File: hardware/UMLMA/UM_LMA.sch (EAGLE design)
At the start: 14 parts, among them IC1 TINY25, J1 AVRISP6_TP

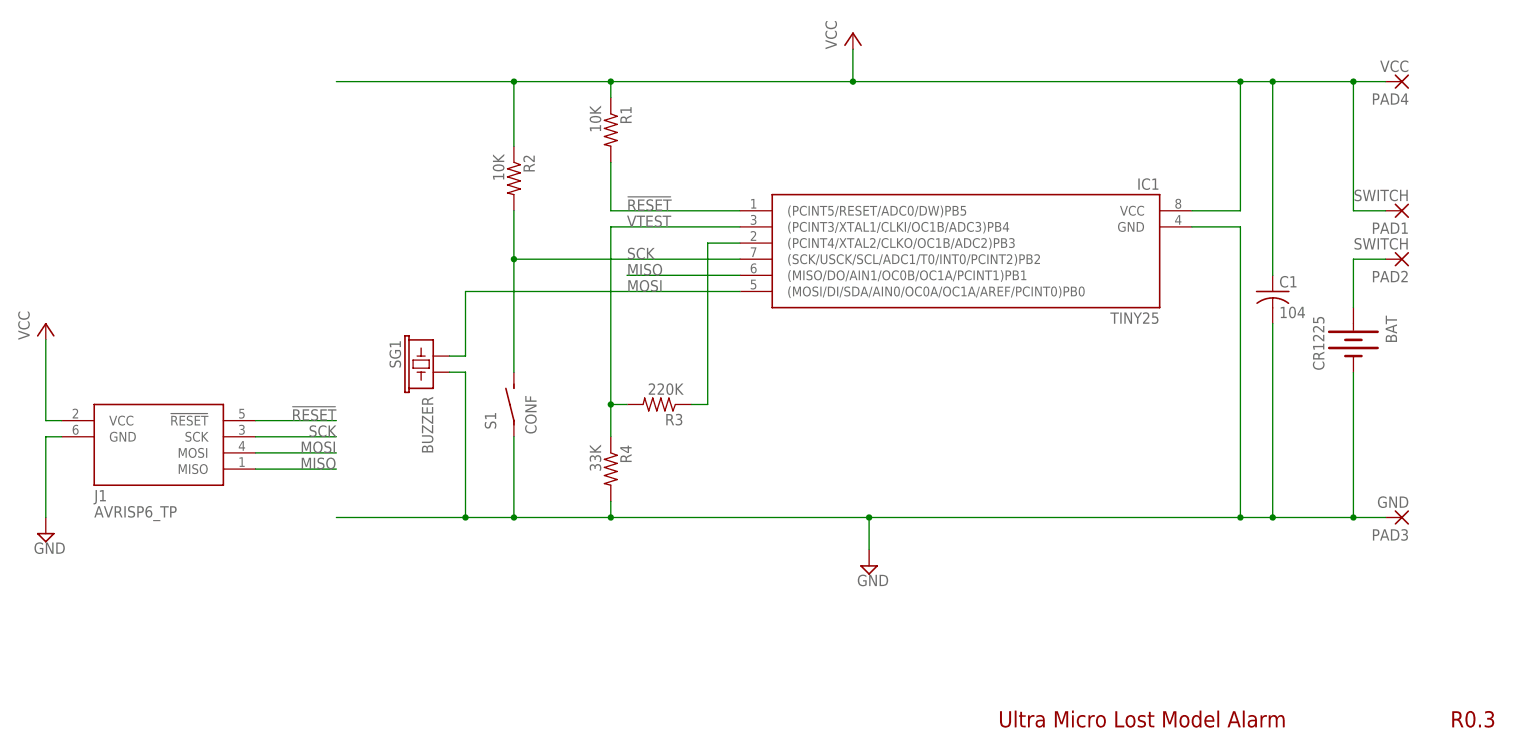
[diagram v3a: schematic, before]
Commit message: Removed extraneous switch pull-up resistor, moved layout and silk labels, increased switch footprint sizes, updated gerbers
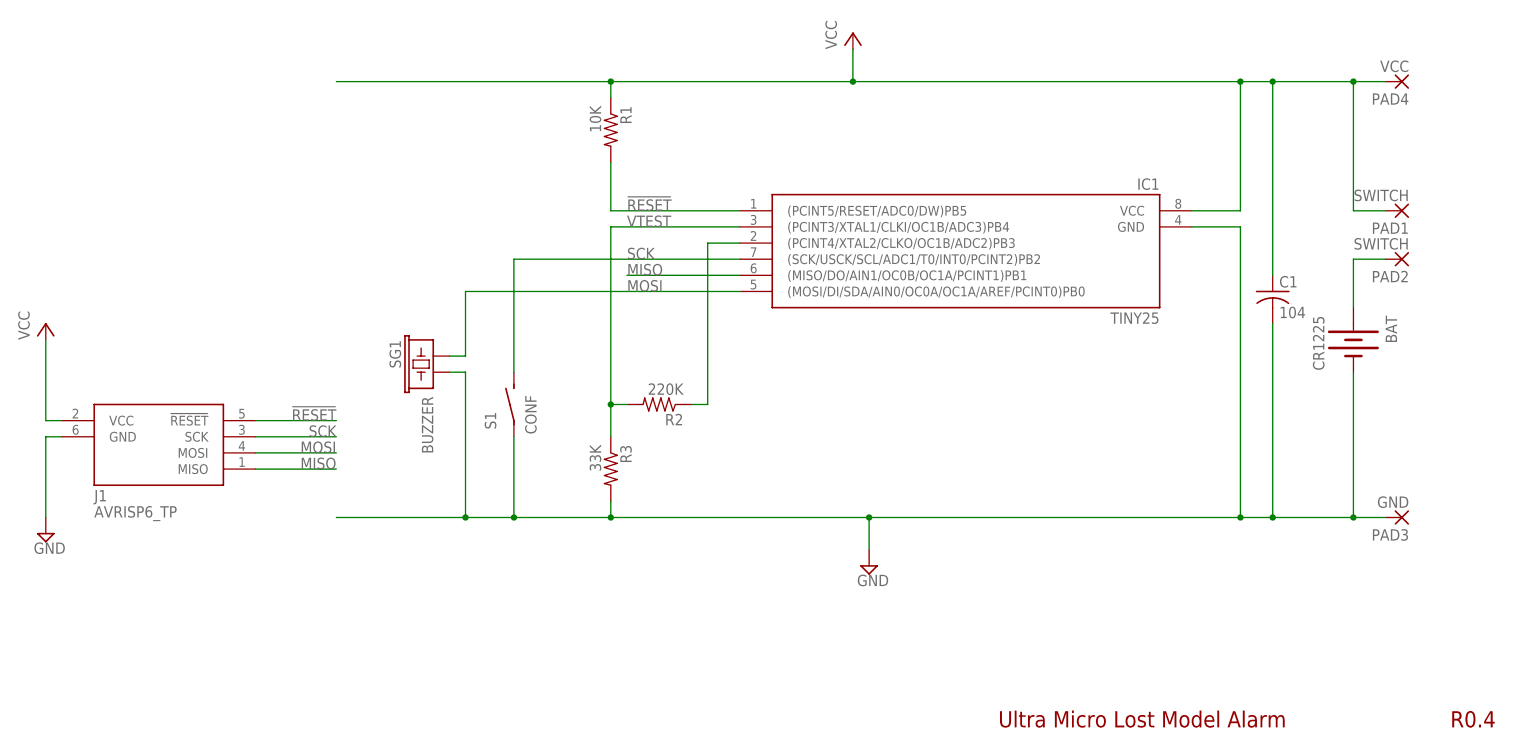
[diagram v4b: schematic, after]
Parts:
- removed R4: 33K, rcl:R-US_R0603
- R2: value 10K -> 220K
- R3: value 220K -> 33K
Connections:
- net GND: now also R3.2; no longer R4.2
- net N$5: now also R2.1; no longer R3.1
- net SCK: no longer R2.2
- net VCC: no longer R2.1
- net VTEST: now also R2.2, R3.1; no longer R3.2, R4.1
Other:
- note added: "R0.4"
- note removed: "R0.3"
- moved on the sheet: R2, R3
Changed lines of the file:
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@@
 <layer number="54" name="bGND_GNDA" color="1" fill="9" visible="no" active="no"/>
 <layer number="56" name="wert" color="7" fill="1" visible="no" active="no"/>
+<layer number="57" name="tCAD" color="7" fill="1" visible="no" active="no"/>
+<layer number="59" name="tCarbon" color="7" fill="1" visible="no" active="no"/>
+<layer number="60" name="bCarbon" color="7" fill="1" visible="no" active="no"/>
+<layer number="90" name="Modules" color="5" fill="1" visible="no" active="no"/>
 <layer number="91" name="Nets" color="2" fill="1" visible="yes" active="yes"/>
 <layer number="92" name="Busses" color="1" fill="1" visible="yes" active="yes"/>
@@
 <layer number="97" name="Info" color="7" fill="1" visible="yes" active="yes"/>
 <layer number="98" name="Guide" color="6" fill="1" visible="yes" active="yes"/>
+<layer number="99" name="SpiceOrder" color="7" fill="1" visible="no" active="no"/>
 <layer number="100" name="Muster" color="7" fill="1" visible="no" active="no"/>
 <layer number="101" name="Hidden" color="15" fill="1" visible="yes" active="yes"/>
@@
 <layer number="106" name="bPlate" color="7" fill="1" visible="yes" active="yes"/>
 <layer number="107" name="Crop" color="7" fill="1" visible="yes" active="yes"/>
+<layer number="108" name="tplace-old" color="10" fill="1" visible="no" active="yes"/>
+<layer number="109" name="ref-old" color="11" fill="1" visible="no" active="yes"/>
+<layer number="110" name="fp0" color="7" fill="1" visible="no" active="yes"/>
+<layer number="111" name="LPC17xx" color="7" fill="1" visible="no" active="yes"/>
+<layer number="113" name="IDFDebug" color="4" fill="1" visible="no" active="yes"/>
 <layer number="116" name="Patch_BOT" color="9" fill="4" visible="yes" active="yes"/>
 <layer number="121" name="_tsilk" color="7" fill="1" visible="yes" active="yes"/>
 <layer number="122" name="_bsilk" color="7" fill="1" visible="yes" active="yes"/>
+<layer number="123" name="tTestmark" color="7" fill="1" visible="no" active="yes"/>
+<layer number="124" name="bTestmark" color="7" fill="1" visible="no" active="yes"/>
 <layer number="125" name="_tNames" color="7" fill="1" visible="no" active="yes"/>
+<layer number="126" name="_bNames" color="7" fill="1" visible="no" active="yes"/>
+<layer number="127" name="_tValues" color="7" fill="1" visible="no" active="yes"/>
+<layer number="128" name="_bValues" color="7" fill="1" visible="no" active="yes"/>
+<layer number="129" name="Mask" color="7" fill="1" visible="no" active="yes"/>
+<layer number="131" name="tAdjust" color="7" fill="1" visible="no" active="yes"/>
+<layer number="132" name="bAdjust" color="7" fill="1" visible="no" active="yes"/>
 <layer number="144" name="Drill_legend" color="7" fill="1" visible="yes" active="yes"/>
+<layer number="150" name="Notes" color="7" fill="1" visible="no" active="yes"/>
 <layer number="151" name="HeatSink" color="7" fill="1" visible="yes" active="yes"/>
+<layer number="152" name="_bDocu" color="7" fill="1" visible="no" active="yes"/>
+<layer number="153" name="FabDoc1" color="7" fill="1" visible="no" active="yes"/>
+<layer number="154" name="FabDoc2" color="7" fill="1" visible="no" active="yes"/>
+<layer number="155" name="FabDoc3" color="7" fill="1" visible="no" active="yes"/>
+<layer number="199" name="Contour" color="7" fill="1" visible="no" active="yes"/>
 <layer number="200" name="200bmp" color="1" fill="10" visible="yes" active="yes"/>
 <layer number="201" name="201bmp" color="2" fill="10" visible="yes" active="yes"/>
@@
 <layer number="223" name="223bmp" color="24" fill="1" visible="no" active="no"/>
 <layer number="224" name="224bmp" color="25" fill="1" visible="no" active="no"/>
+<layer number="225" name="225bmp" color="7" fill="1" visible="no" active="yes"/>
+<layer number="226" name="226bmp" color="7" fill="1" visible="no" active="yes"/>
+<layer number="227" name="227bmp" color="7" fill="1" visible="no" active="yes"/>
+<layer number="228" name="228bmp" color="7" fill="1" visible="no" active="yes"/>
+<layer number="229" name="229bmp" color="7" fill="1" visible="no" active="yes"/>
+<layer number="230" name="230bmp" color="7" fill="1" visible="no" active="yes"/>
 <layer number="231" name="Eagle3D_PG1" color="14" fill="1" visible="yes" active="yes"/>
 <layer number="232" name="Eagle3D_PG2" color="14" fill="2" visible="yes" active="yes"/>
 <layer number="233" name="Eagle3D_PG3" color="14" fill="4" visible="yes" active="yes"/>
+<layer number="248" name="Housing" color="7" fill="1" visible="no" active="yes"/>
+<layer number="249" name="Edge" color="7" fill="1" visible="no" active="yes"/>
 <layer number="250" name="Descript" color="3" fill="1" visible="no" active="no"/>
 <layer number="251" name="SMDround" color="12" fill="11" visible="no" active="no"/>
 <layer number="254" name="cooling" color="7" fill="1" visible="yes" active="yes"/>
+<layer number="255" name="routoute" color="7" fill="1" visible="no" active="yes"/>
 </layers>
 <schematic xreflabel="%F%N/%S.%C%R" xrefpart="/%S.%C%R">
@@
 <attribute name="BOM" value="EXCLUDE"/>
 </part>
-<part name="R3" library="rcl" deviceset="R-US_" device="R0603" value="220K">
+<part name="R2" library="rcl" deviceset="R-US_" device="R0603" value="220K">
 <attribute name="PARTNO" value="ERJ-3GEYJ102V"/>
 </part>
-<part name="R4" library="rcl" deviceset="R-US_" device="R0603" value="33K">
+<part name="R3" library="rcl" deviceset="R-US_" device="R0603" value="33K">
 <attribute name="PARTNO" value="ERJ-3GEYJ102V"/>
 </part>
@@
 <part name="SUPPLY2" library="supply2" deviceset="GND" device=""/>
 <part name="P+2" library="supply1" deviceset="VCC" device=""/>
-<part name="R2" library="rcl" deviceset="R-US_" device="R0603" value="10K">
-<attribute name="PARTNO" value="ERJ-3GEYJ102V"/>
-</part>
 <part name="S1" library="bt_electromech" deviceset="SPST" device="_3X4X2" value="CONF"/>
 <part name="IC1" library="bt_avr" deviceset="TINY25" device="-20SSU" value="TINY25"/>
@@
 <plain>
 <text x="160.02" y="25.4" size="2.54" layer="94">Ultra Micro Lost Model Alarm</text>
-<text x="231.14" y="25.4" size="2.54" layer="94">R0.3</text>
+<text x="231.14" y="25.4" size="2.54" layer="94">R0.4</text>
 </plain>
 <instances>
@@
 <attribute name="BOM" x="223.52" y="99.06" size="1.778" layer="96" display="off"/>
 </instance>
-<instance part="R3" gate="G$1" x="106.68" y="76.2" rot="R180">
+<instance part="R2" gate="G$1" x="106.68" y="76.2" rot="R180">
 <attribute name="PARTNO" x="106.68" y="76.2" size="1.778" layer="96" rot="R270" display="off"/>
 </instance>
-<instance part="R4" gate="G$1" x="99.06" y="66.04" rot="R270">
+<instance part="R3" gate="G$1" x="99.06" y="66.04" rot="R270">
 <attribute name="PARTNO" x="99.06" y="66.04" size="1.778" layer="96" display="off"/>
 </instance>
@@
 <instance part="SUPPLY2" gate="GND" x="10.16" y="55.88"/>
 <instance part="P+2" gate="VCC" x="10.16" y="88.9"/>
-<instance part="R2" gate="G$1" x="83.82" y="111.76" rot="R270">
-<attribute name="PARTNO" x="83.82" y="111.76" size="1.778" layer="96" display="off"/>
-</instance>
 <instance part="S1" gate="G$1" x="83.82" y="76.2" rot="R90"/>
 <instance part="IC1" gate="1" x="154.94" y="99.06" rot="MR0"/>
@@
 <wire x1="137.16" y1="127" x2="99.06" y2="127" width="0.1524" layer="91"/>
 <wire x1="99.06" y1="124.46" x2="99.06" y2="127" width="0.1524" layer="91"/>
-<wire x1="55.88" y1="127" x2="83.82" y2="127" width="0.1524" layer="91"/>
-<wire x1="83.82" y1="127" x2="99.06" y2="127" width="0.1524" layer="91"/>
+<wire x1="55.88" y1="127" x2="99.06" y2="127" width="0.1524" layer="91"/>
 <junction x="203.2" y="127"/>
 <junction x="137.16" y="127"/>
@@
 <pinref part="R1" gate="G$1" pin="1"/>
 <pinref part="PAD1" gate="G$1" pin="P"/>
-<pinref part="R2" gate="G$1" pin="1"/>
-<wire x1="83.82" y1="116.84" x2="83.82" y2="127" width="0.1524" layer="91"/>
-<junction x="83.82" y="127"/>
 <pinref part="IC1" gate="1" pin="VCC"/>
 <wire x1="190.5" y1="106.68" x2="198.12" y2="106.68" width="0.1524" layer="91"/>
@@
 <pinref part="SUPPLY1" gate="GND" pin="GND"/>
 <pinref part="SG1" gate="G$1" pin="2"/>
-<pinref part="R4" gate="G$1" pin="2"/>
+<pinref part="R3" gate="G$1" pin="2"/>
 <pinref part="BAT" gate="G$1" pin="-"/>
 <pinref part="S1" gate="G$1" pin="P"/>
@@
 <wire x1="83.82" y1="99.06" x2="119.38" y2="99.06" width="0.1524" layer="91"/>
 <wire x1="83.82" y1="81.28" x2="83.82" y2="99.06" width="0.1524" layer="91"/>
-<junction x="83.82" y="99.06"/>
-<pinref part="R2" gate="G$1" pin="2"/>
-<wire x1="83.82" y1="99.06" x2="83.82" y2="106.68" width="0.1524" layer="91"/>
 <pinref part="IC1" gate="1" pin="(SCK/USCK/SCL/ADC1/T0/INT0/PCINT2)PB2"/>
 </segment>
@@
 <wire x1="99.06" y1="76.2" x2="101.6" y2="76.2" width="0.1524" layer="91"/>
 <junction x="99.06" y="76.2"/>
-<pinref part="R4" gate="G$1" pin="1"/>
-<pinref part="R3" gate="G$1" pin="2"/>
+<pinref part="R3" gate="G$1" pin="1"/>
+<pinref part="R2" gate="G$1" pin="2"/>
 <label x="101.6" y="104.14" size="1.778" layer="95"/>
 <pinref part="IC1" gate="1" pin="(PCINT3/XTAL1/CLKI/OC1B/ADC3)PB4"/>
@@
 <wire x1="114.3" y1="76.2" x2="114.3" y2="101.6" width="0.1524" layer="91"/>
 <wire x1="114.3" y1="101.6" x2="119.38" y2="101.6" width="0.1524" layer="91"/>
-<pinref part="R3" gate="G$1" pin="1"/>
+<pinref part="R2" gate="G$1" pin="1"/>
 <pinref part="IC1" gate="1" pin="(PCINT4/XTAL2/CLKO/OC1B/ADC2)PB3"/>
 </segment>
